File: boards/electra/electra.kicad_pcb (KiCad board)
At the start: 2 copper layers, 165 x 75 mm, 60 parts, among them IC1 ATTINY85-P, P1 Bat1, P2 Bat2, SW1 SW_PSXXX, SW2 Kb, SW3 Kb, SW4 Kb, SW5 Kb, SW6 Kb, SW7 Kb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

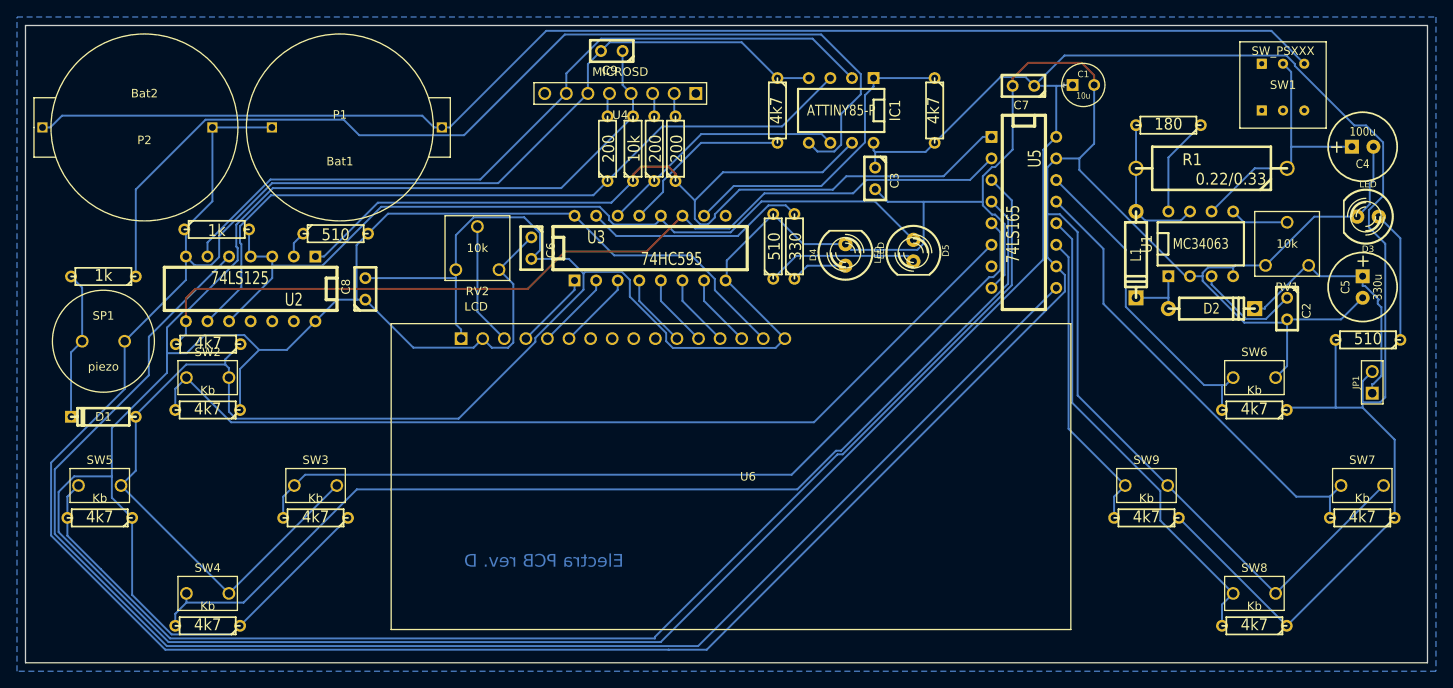
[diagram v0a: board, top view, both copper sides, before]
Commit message: Electra PCB optimized.
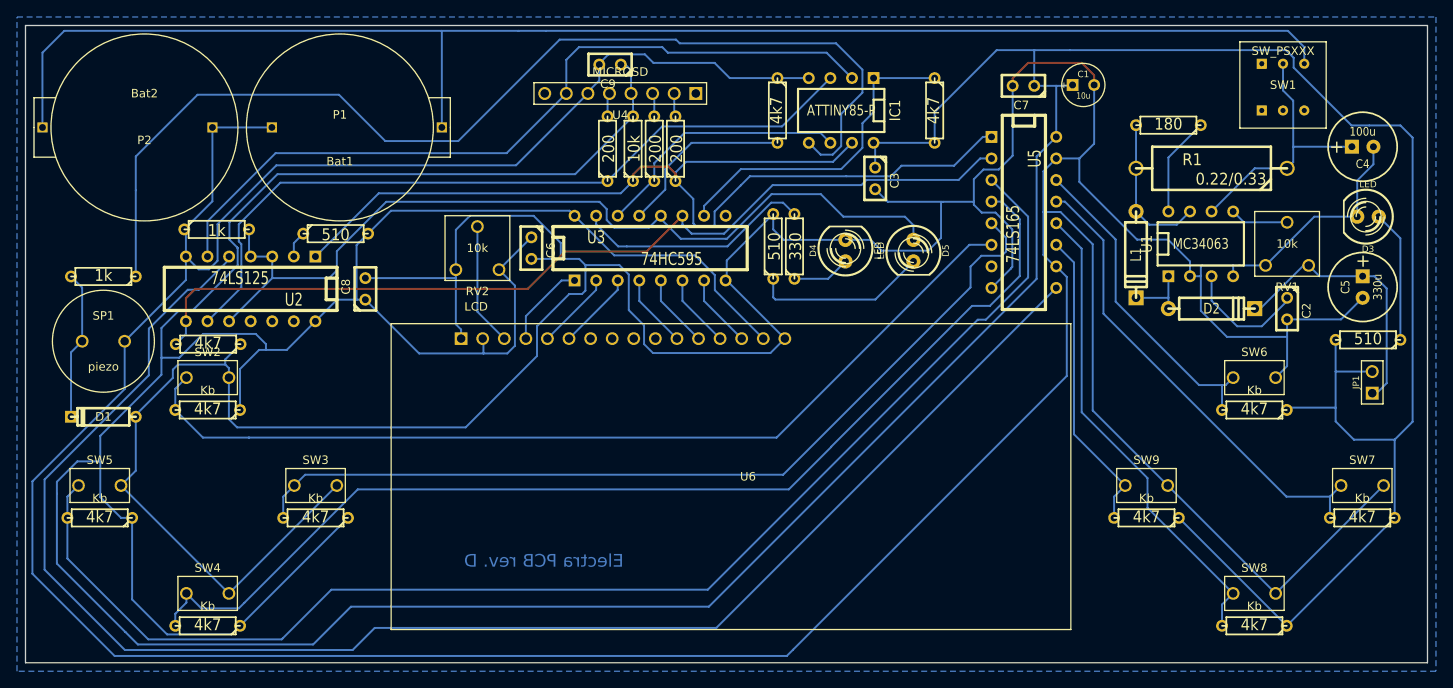
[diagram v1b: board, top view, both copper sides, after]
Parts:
- moved C9 1.61 mm to (138.8, 54.6)
- moved D4 0.50 mm to (166.5, 76.5)
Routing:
- net GND: track 771.5 -> 804.3 mm
- net +3.3V: track 634.4 -> 657.9 mm
- net N-0000038: track 156.0 -> 172.5 mm
- net N-0000031: track 120.4 -> 126.2 mm
- net N-0000053: track 99.7 -> 105.4 mm
- net N-0000016: track 181.9 -> 187.2 mm
- net N-0000044: track 153.3 -> 157.0 mm
- net N-0000028: track 114.8 -> 118.1 mm
- net N-0000043: track 127.1 -> 130.2 mm
- net N-0000019: track 17.9 -> 20.6 mm
- net N-0000024: track 12.6 -> 14.5 mm
- net N-000006: track 26.2 -> 28.1 mm
- net N-0000029: track 90.7 -> 92.3 mm
- net N-0000025: track 30.9 -> 32.3 mm
- net N-000002: track 29.4 -> 30.8 mm
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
